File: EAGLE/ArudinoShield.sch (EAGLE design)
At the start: 25 parts, among them IC1 L298, U1 REG1117

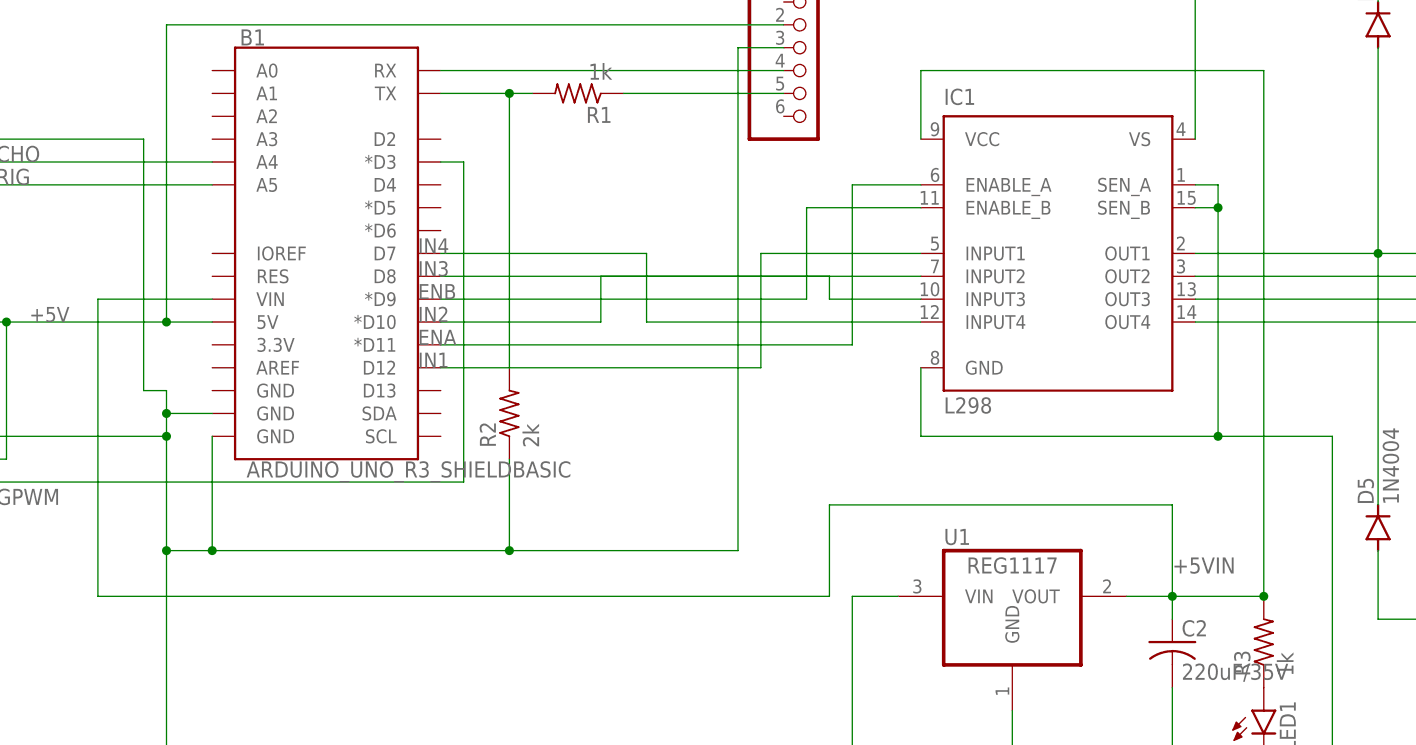
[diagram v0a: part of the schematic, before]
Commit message: updated to power peripherals from regulator, updated line width
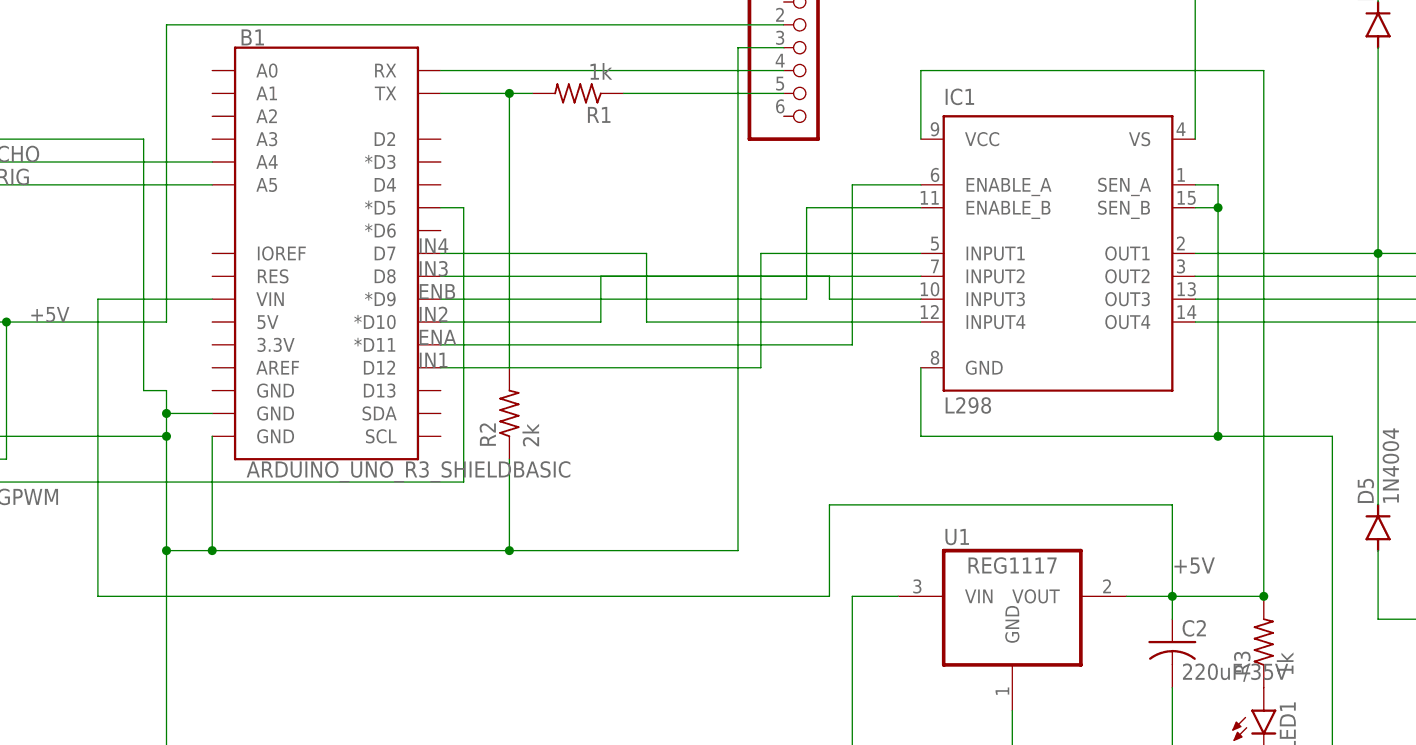
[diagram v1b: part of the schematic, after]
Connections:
- removed net +5VIN: B1.VIN, C2.1, IC1.VCC, R3.2, U1.VOUT
- net +5V: now also B1.VIN, C2.1, IC1.VCC, R3.2, U1.VOUT; no longer B1.5V
- net 9GPWM: now also B1.*D5; no longer B1.*D3
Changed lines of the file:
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@@
 <net name="+5V" class="0">
 <segment>
-<pinref part="B1" gate="G$1" pin="5V"/>
-<wire x1="50.8" y1="43.18" x2="45.72" y2="43.18" width="0.1524" layer="91"/>
 <wire x1="45.72" y1="43.18" x2="27.94" y2="43.18" width="0.1524" layer="91"/>
 <wire x1="27.94" y1="43.18" x2="25.4" y2="43.18" width="0.1524" layer="91"/>
@@
 <wire x1="114.3" y1="76.2" x2="45.72" y2="76.2" width="0.1524" layer="91"/>
 <wire x1="45.72" y1="76.2" x2="45.72" y2="43.18" width="0.1524" layer="91"/>
-<junction x="45.72" y="43.18"/>
 <pinref part="HC-SR04" gate="A" pin="1"/>
 <wire x1="25.4" y1="55.88" x2="20.32" y2="55.88" width="0.1524" layer="91"/>
@@
 <wire x1="27.94" y1="27.94" x2="27.94" y2="43.18" width="0.1524" layer="91"/>
 <junction x="27.94" y="43.18"/>
+</segment>
+<segment>
+<pinref part="R3" gate="G$1" pin="2"/>
+<pinref part="C2" gate="G$1" pin="1"/>
+<wire x1="157.48" y1="12.7" x2="152.4" y2="12.7" width="0.1524" layer="91"/>
+<wire x1="157.48" y1="10.16" x2="157.48" y2="12.7" width="0.1524" layer="91"/>
+<junction x="157.48" y="12.7"/>
+<pinref part="U1" gate="G$1" pin="VOUT"/>
+<pinref part="B1" gate="G$1" pin="VIN"/>
+<wire x1="50.8" y1="45.72" x2="38.1" y2="45.72" width="0.1524" layer="91"/>
+<wire x1="38.1" y1="45.72" x2="38.1" y2="12.7" width="0.1524" layer="91"/>
+<wire x1="38.1" y1="12.7" x2="119.38" y2="12.7" width="0.1524" layer="91"/>
+<wire x1="119.38" y1="12.7" x2="119.38" y2="22.86" width="0.1524" layer="91"/>
+<wire x1="119.38" y1="22.86" x2="157.48" y2="22.86" width="0.1524" layer="91"/>
+<wire x1="157.48" y1="22.86" x2="157.48" y2="12.7" width="0.1524" layer="91"/>
+<wire x1="157.48" y1="12.7" x2="167.64" y2="12.7" width="0.1524" layer="91"/>
+<wire x1="167.64" y1="12.7" x2="167.64" y2="71.12" width="0.1524" layer="91"/>
+<wire x1="167.64" y1="71.12" x2="129.54" y2="71.12" width="0.1524" layer="91"/>
+<pinref part="IC1" gate="L298" pin="VCC"/>
+<wire x1="129.54" y1="71.12" x2="129.54" y2="63.5" width="0.1524" layer="91"/>
+<label x="157.48" y="15.24" size="1.778" layer="95"/>
+<junction x="167.64" y="12.7"/>
 </segment>
 </net>
@@
 <wire x1="20.32" y1="25.4" x2="78.74" y2="25.4" width="0.1524" layer="91"/>
 <label x="25.4" y="22.86" size="1.778" layer="95"/>
-<wire x1="78.74" y1="25.4" x2="78.74" y2="60.96" width="0.1524" layer="91"/>
-<pinref part="B1" gate="G$1" pin="*D3"/>
-<wire x1="78.74" y1="60.96" x2="76.2" y2="60.96" width="0.1524" layer="91"/>
+<wire x1="78.74" y1="25.4" x2="78.74" y2="55.88" width="0.1524" layer="91"/>
+<pinref part="B1" gate="G$1" pin="*D5"/>
+<wire x1="76.2" y1="55.88" x2="78.74" y2="55.88" width="0.1524" layer="91"/>
 </segment>
 </net>
-<net name="+5VIN" class="0">
-<segment>
-<pinref part="R3" gate="G$1" pin="2"/>
-<pinref part="C2" gate="G$1" pin="1"/>
-<wire x1="157.48" y1="12.7" x2="152.4" y2="12.7" width="0.1524" layer="91"/>
-<wire x1="157.48" y1="10.16" x2="157.48" y2="12.7" width="0.1524" layer="91"/>
-<junction x="157.48" y="12.7"/>
-<pinref part="U1" gate="G$1" pin="VOUT"/>
-<pinref part="B1" gate="G$1" pin="VIN"/>
-<wire x1="50.8" y1="45.72" x2="38.1" y2="45.72" width="0.1524" layer="91"/>
-<wire x1="38.1" y1="45.72" x2="38.1" y2="12.7" width="0.1524" layer="91"/>
-<wire x1="38.1" y1="12.7" x2="119.38" y2="12.7" width="0.1524" layer="91"/>
-<wire x1="119.38" y1="12.7" x2="119.38" y2="22.86" width="0.1524" layer="91"/>
-<wire x1="119.38" y1="22.86" x2="157.48" y2="22.86" width="0.1524" layer="91"/>
-<wire x1="157.48" y1="22.86" x2="157.48" y2="12.7" width="0.1524" layer="91"/>
-<wire x1="157.48" y1="12.7" x2="167.64" y2="12.7" width="0.1524" layer="91"/>
-<wire x1="167.64" y1="12.7" x2="167.64" y2="71.12" width="0.1524" layer="91"/>
-<wire x1="167.64" y1="71.12" x2="129.54" y2="71.12" width="0.1524" layer="91"/>
-<pinref part="IC1" gate="L298" pin="VCC"/>
-<wire x1="129.54" y1="71.12" x2="129.54" y2="63.5" width="0.1524" layer="91"/>
-<label x="157.48" y="15.24" size="1.778" layer="95"/>
-<junction x="167.64" y="12.7"/>
-</segment>
-</net>
